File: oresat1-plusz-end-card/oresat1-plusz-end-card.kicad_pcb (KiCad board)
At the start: 4 copper layers, 99.8 x 94.6 mm, 45 parts, among them J1 J-SAMTEC-TFM-120-01-L-D-RA, J2 Harwin M55-7101242R, J3 Harwin M55-7101242R, J4 Harwin M55-7101242R, J5 Harwin M55-7101242R, J6 Conn_Coaxial

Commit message: v1.1, theoretically done
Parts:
- added C10: 100n, oresat-passives:0603-C-NOSILK, F.Cu at (116.2, 120.6)
- added C22: 1u, oresat-passives:0603-C-NOSILK, F.Cu at (114.2, 115.9)
- added C23: 1u, oresat-passives:0603-C-NOSILK, F.Cu at (111.3, 115.9)
- added C3: 100n, oresat-passives:0603-C-NOSILK, F.Cu at (116.2, 126.6)
- added D14: 1N4151WS, Diode_SMD:D_SOD-323, F.Cu at (124.5, 136.8)
- added Q1: DMP2240UDM, Package_TO_SOT_SMD:SOT-23-6, F.Cu at (113.2, 125.1)
- added Q11: DMP2240UDM-7, Package_TO_SOT_SMD:SOT-23-6, F.Cu at (138.3, 139.4)
- added Q2: PMV45EN, Package_TO_SOT_SMD:SOT-23-3, F.Cu at (117.1, 139.3)
- added Q3: PMV45EN, Package_TO_SOT_SMD:SOT-23-3, F.Cu at (118.2, 136.1)
- added Q4: PMV45EN, Package_TO_SOT_SMD:SOT-23-3, F.Cu at (113.6, 139.2)
- added Q6: PMV45EN, Package_TO_SOT_SMD:SOT-23-3, F.Cu at (114.8, 136.1)
- added Q9: DMP2240UDM-7, Package_TO_SOT_SMD:SOT-23-6, F.Cu at (133.7, 139.4)
- added R100: 1k, Resistor_SMD:R_0603_1608Metric, F.Cu at (122.2, 135.9)
- added R101: 47k, Resistor_SMD:R_0603_1608Metric, F.Cu at (124.7, 135.0)
- added R102: 10k, Resistor_SMD:R_0603_1608Metric, F.Cu at (124.7, 133.5)
- added R24: 10, oresat-passives:0603-C-NOSILK, F.Cu at (110.3, 126.5)
- added R39: 1k, oresat-passives:0603-C-NOSILK, F.Cu at (110.8, 130.5)
- added R40: 1k, oresat-passives:0603-C-NOSILK, F.Cu at (109.8, 128.3)
- added R45: 1k, oresat-passives:0603-C-NOSILK, F.Cu at (109.8, 130.5)
- added R46: 1k, oresat-passives:0603-C-NOSILK, F.Cu at (110.8, 128.3)
- added R52: 1k, oresat-passives:0603-C-NOSILK, F.Cu at (110.8, 134.9)
- added R53: 1k, oresat-passives:0603-C-NOSILK, F.Cu at (109.8, 132.7)
- added R54: 1k, oresat-passives:0603-C-NOSILK, F.Cu at (109.8, 134.9)
- added R55: 1k, oresat-passives:0603-C-NOSILK, F.Cu at (110.8, 132.7)
- added R56: 1k, oresat-passives:0603-C-NOSILK, F.Cu at (110.8, 139.3)
- added R57: 1k, oresat-passives:0603-C-NOSILK, F.Cu at (109.8, 137.1)
- added R58: 1k, oresat-passives:0603-C-NOSILK, F.Cu at (109.8, 139.3)
- added R59: 1k, oresat-passives:0603-C-NOSILK, F.Cu at (110.8, 137.1)
- added R60: 100, oresat-passives:0603-C-NOSILK, F.Cu at (110.3, 125.2)
- added R61: 10k, oresat-passives:0603-C-NOSILK, F.Cu at (116.3, 125.5)
- added R77: 665k, oresat-passives:0603-C-NOSILK, F.Cu at (113.7, 122.5)
- added R78: 330k, oresat-passives:0603-C-NOSILK, F.Cu at (114.2, 117.0)
- added R79: 1M, oresat-passives:0603-C-NOSILK, F.Cu at (114.2, 118.1)
- added R80: 100, oresat-passives:0603-C-NOSILK, F.Cu at (110.3, 124.0)
- added R81: 665k, oresat-passives:0603-C-NOSILK, F.Cu at (111.5, 122.5)
- added R82: 330k, oresat-passives:0603-C-NOSILK, F.Cu at (111.3, 117.0)
- added R83: 1M, oresat-passives:0603-C-NOSILK, F.Cu at (111.3, 118.1)
- added R97: 10k, Resistor_SMD:R_0603_1608Metric, F.Cu at (116.4, 133.2)
- added R98: 10k, Resistor_SMD:R_0603_1608Metric, F.Cu at (113.4, 133.2)
- added R99: 10k, Resistor_SMD:R_0603_1608Metric, F.Cu at (130.4, 139.2)
- added TP1: Test-Point, oresat-misc:TestPoint_Pad_D1.0mm, F.Cu at (140.0, 134.0)
- added TP111: Test-Point, oresat-misc:TestPoint_Pad_D1.0mm, F.Cu at (118.8, 131.8)
- added TP112: Test-Point, oresat-misc:TestPoint_Pad_D1.0mm, F.Cu at (118.8, 130.2)
- added TP35: Test-Point, oresat-misc:TestPoint-0.75mm-th, F.Cu at (109.1, 121.5)
- added TP37: Test-Point, oresat-misc:TestPoint-0.75mm-th, F.Cu at (116.5, 124.1)
- added TP38: Test-Point, oresat-misc:TestPoint-0.75mm-th, F.Cu at (116.5, 122.5)
- added TP63: Test-Point, oresat-misc:TestPoint_Pad_D1.0mm, F.Cu at (118.8, 128.8)
- added U11: MIC842LYC5, Package_TO_SOT_SMD:SOT-353_SC-70-5, F.Cu at (111.4, 120.3)
- added U12: MIC842LYC5, Package_TO_SOT_SMD:SOT-353_SC-70-5, F.Cu at (114.3, 120.3)
- added U2: MAX7310, Package_DFN_QFN:QFN-16-1EP_4x4mm_P0.65mm_EP2.1x2.1mm, F.Cu at (115.2, 129.9)
- moved R1 20.1 mm to (148.5, 130.6), turned to -102.2 degrees
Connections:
- J1 pad 10: unconnected-(J1-Pad10) -> OPD_SDA
- J1 pad 11: unconnected-(J1-Pad11) -> OPD_SDA
- J1 pad 12: unconnected-(J1-Pad12) -> OPD_SCL
- J1 pad 13: unconnected-(J1-Pad13) -> OPD_SCL
- J1 pad 14: unconnected-(J1-Pad14) -> OPD_PWR
- J1 pad 15: unconnected-(J1-Pad15) -> OPD_PWR
- J1 pad 7: /HELICAL-DEPLOY -> unconnected-(J1-Pad7)
- J1 pad 8: /HELICAL-DEPLOY -> unconnected-(J1-Pad8)
- R1 pad 2: /HELICAL-DEPLOY -> /OPD/HELICAL_DEPLOY
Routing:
- net OPD_PWR: track 0.00 -> 80.8 mm, vias 0 -> 3
- net OPD_SDA: track 0.00 -> 77.9 mm, vias 0 -> 1
- net OPD_SCL: track 0.00 -> 76.4 mm, vias 0 -> 1
- net VPD: track 0.00 -> 47.7 mm, vias 0 -> 4
- net /OPD/OPD-SCL-INT: track 0.00 -> 39.6 mm, vias 0 -> 6
- net Net-(Q11A-G): track 0.00 -> 33.6 mm, vias 0 -> 7
- net /OPD/OPD-SDA-INT: track 0.00 -> 30.9 mm, vias 0 -> 5
- net /OPD/FIRE_HELICAL_2: track 0.00 -> 19.2 mm, vias 0 -> 2
- net /OPD/FIRE_HELICAL_1: track 0.00 -> 16.0 mm, vias 0 -> 3
- net /OPD/AD2: track 0.00 -> 13.4 mm, vias 0 -> 2
- net /OPD/HELICAL_DEPLOY: track 0.00 -> 12.7 mm
- net /OPD/READ_HELICAL: track 0.00 -> 12.1 mm
- net /OPD/AD1: track 0.00 -> 9.28 mm, vias 0 -> 2
- net /OPD/TEST_HELICAL: track 0.00 -> 7.38 mm, vias 0 -> 2
- net Net-(Q4-S): track 0.00 -> 6.46 mm, vias 0 -> 2
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- added copper zone on F.Cu, net /OPD/HELICAL_DEPLOY
- removed copper zone on B.Cu, net /HELICAL-DEPLOY
- removed copper zone on F.Cu, net /HELICAL-DEPLOY
- removed copper zone on In2.Cu, net /HELICAL-DEPLOY
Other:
- board text added: "${TITLE}"
- board text removed: "OreSat0.5 +Z End Card"

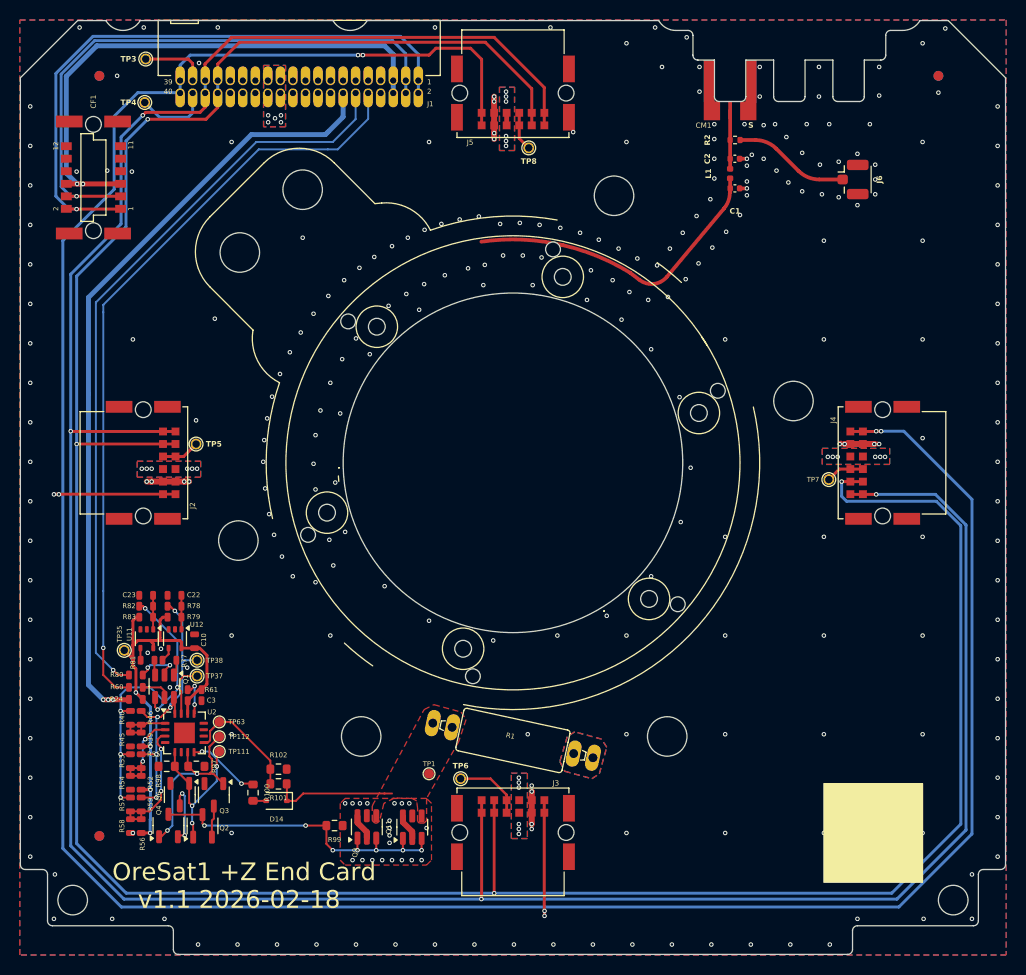
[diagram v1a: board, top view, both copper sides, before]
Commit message: Changed symbols & fab layout
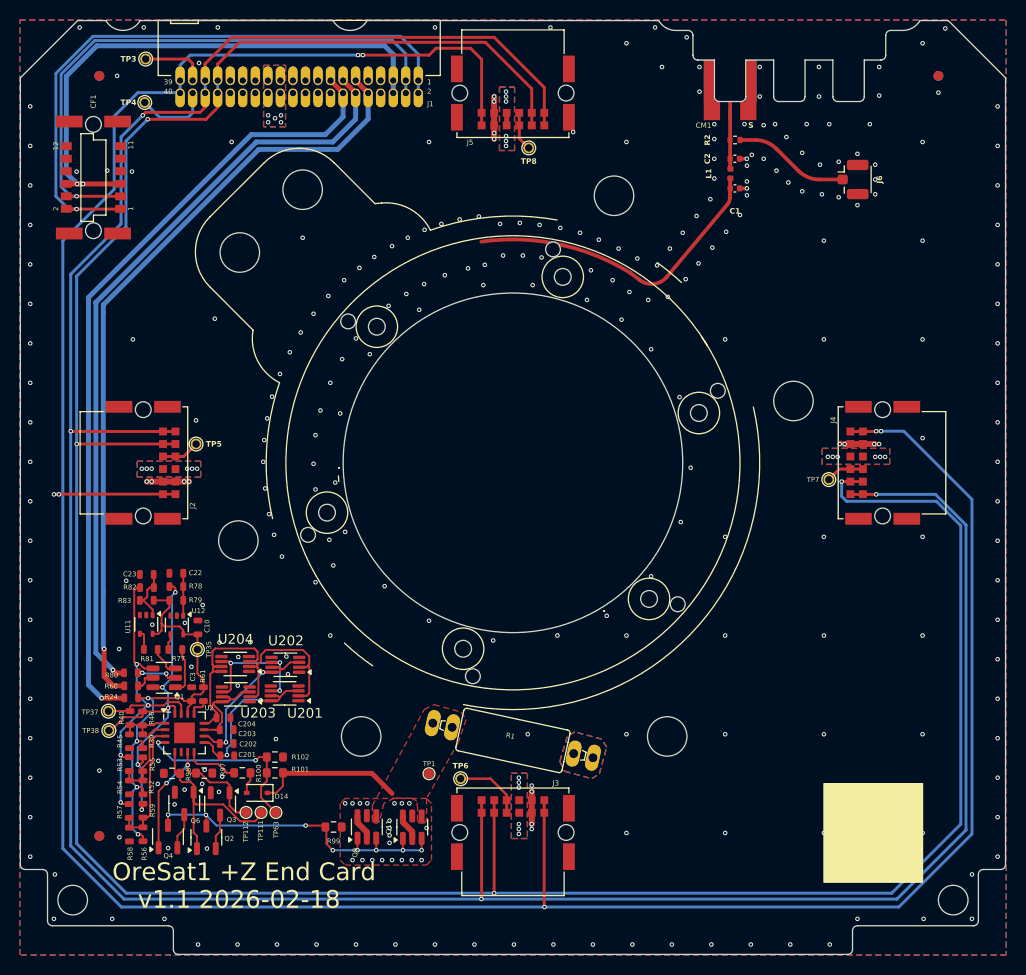
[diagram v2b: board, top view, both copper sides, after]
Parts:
- added C201: 100n, oresat-passives:0603-C-NOSILK, F.Cu at (119.6, 132.2)
- added C202: 100n, oresat-passives:0603-C-NOSILK, F.Cu at (119.5, 130.9)
- added C203: 100n, oresat-passives:0603-C-NOSILK, F.Cu at (119.5, 129.5)
- added C204: 100n, oresat-passives:0603-C-NOSILK, F.Cu at (119.2, 128.3)
- added U201: TS5A21366, Package_SO:VSSOP-8_2.3x2mm_P0.5mm, F.Cu at (125.4, 125.9)
- added U202: TS5A21366, Package_SO:VSSOP-8_2.3x2mm_P0.5mm, F.Cu at (125.4, 123.0)
- added U203: TS5A21366, Package_SO:VSSOP-8_2.3x2mm_P0.5mm, F.Cu at (120.4, 126.0)
- added U204: TS5A21366, Package_SO:VSSOP-8_2.3x2mm_P0.5mm, F.Cu at (120.4, 122.9)
- CF1: value J-HARWIN-M55-6001242R -> M55-6001242R
- CM1: value J-MOLEX-SMPM-73300-003X -> 2477330-1
- J2, J3, J4, J5: value Harwin M55-7101242R -> M55-7101242R
- J6: value Conn_Coaxial -> U.FL-R-SMT-1
- moved TP38 11.4 mm to (107.6, 129.6)
- moved TP63 10.8 mm to (124.5, 137.9), turned to 180 degrees
- moved TP37 9.66 mm to (107.5, 127.7)
- moved TP112 8.14 mm to (121.5, 137.9), turned to 180 degrees
- moved TP111 7.49 mm to (123.0, 137.9), turned to 180 degrees
- moved TP35 7.41 mm to (116.5, 121.4)
- moved R100 2.28 mm to (121.1, 133.9), turned to 0 degrees
- moved C22 2.24 mm to (114.4, 113.7)
- moved D14 2.13 mm to (122.6, 135.9)
- moved C23 2.11 mm to (111.4, 113.8)
- moved R78 2.00 mm to (114.4, 115.0)
- moved R82 1.89 mm to (111.4, 115.1)
- moved R79 1.71 mm to (114.4, 116.4)
- moved R83 1.71 mm to (111.4, 116.4), turned to 0 degrees
- moved U11 1.45 mm to (111.4, 118.9)
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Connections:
- U2 pad 10: unconnected-(U2-IO5-Pad10) -> /OPD/PY_UART_EN
- U2 pad 11: unconnected-(U2-IO6-Pad11) -> /OPD/MX_UART_EN
- U2 pad 12: unconnected-(U2-IO7-Pad12) -> /OPD/MY_UART_EN
- U2 pad 4: unconnected-(U2-IO0-Pad4) -> /OPD/READ_HELICAL
- U2 pad 9: /OPD/READ_HELICAL -> /OPD/PX_UART_EN
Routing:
- net /OPD/C3-UART-TX: track 0.00 -> 17.4 mm
- net /OPD/MY_UART_EN: track 0.00 -> 16.9 mm
- net /OPD/PX_UART_EN: track 0.00 -> 16.5 mm, vias 0 -> 2
- net /OPD/PY_UART_EN: track 0.00 -> 16.4 mm, vias 0 -> 2
- net /OPD/C3-UART-RX: track 0.00 -> 14.3 mm, vias 0 -> 3
- net /OPD/MX_UART_EN: track 0.00 -> 9.92 mm
- net /OPD/READ_HELICAL: track 12.1 -> 19.2 mm, vias 0 -> 2
- net /OPD/OPD-SDA-INT: track 30.9 -> 36.7 mm
- net /OPD/FIRE_HELICAL_1: track 16.0 -> 20.6 mm, vias 3 -> 0
- net VPD: track 47.7 -> 44.5 mm
- net Net-(Q1A-G): track 1.60 -> 4.77 mm
- net Net-(Q4-S): track 6.46 -> 3.65 mm, vias 2 -> 0
- net /OPD/OPD-SCL-INT: track 39.6 -> 36.8 mm, vias 6 -> 4
- net /OPD/HELICAL_DEPLOY: track 12.7 -> 15.1 mm
- net Net-(U11-INP): track 3.45 -> 5.55 mm
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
